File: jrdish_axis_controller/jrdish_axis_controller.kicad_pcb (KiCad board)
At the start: 2 copper layers, 114 parts, among them CN1 KF2EDGR-2.54-9P, CN2 KF2EDGR-2.54-6P, CN3 KF2EDGR-2.54-4P, CN4 KF2EDGR-2.54-4P, CN5 KF2EDGR-2.54-2P, CN6 KF2EDGR-2.54-2P, CN7 SM04B-SRSS-TB (LF)(SN), CN8 SM04B-SRSS-TB (LF)(SN), J1 Conn_ARM_SWD_TagConnect_TC2030, M1 MountingHole_2.7mm_M2.5_ISO14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, Q1 AO3407A, Q2 AO3400A, SW1 DSHP04TSGER, SW2 SS-12F49-G050, U1 STM32G474CET6, U2 ISOW1432BDFMR, U3 MP2322GQH-Z, U4 LTC4311ISC6#TRPBF, U5 LM75BIMX-5/NOPB, U6 M24C64-RMN6TP, X1 NX2016SA-16MHZ-EXS00A-CS07826

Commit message: PCB layout in progress
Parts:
- moved H2 8.57 mm to (163.5, 75.7), turned to 90 degrees
- moved R21 6.60 mm to (128.7, 113.7)
- moved C32 6.60 mm to (132.1, 115.0)
- moved C34 6.60 mm to (137.1, 114.5)
- moved C35 6.60 mm to (135.6, 114.5)
- moved C36 6.60 mm to (130.1, 110.7)
- moved C37 6.60 mm to (133.3, 117.5)
- moved C38 6.60 mm to (134.3, 112.5)
- moved L5 6.60 mm to (129.3, 117.2)
- moved R20 6.60 mm to (128.6, 112.2)
- moved R22 6.60 mm to (131.6, 112.5)
- moved U3 6.60 mm to (133.8, 114.3)
- moved C33 6.45 mm to (138.7, 114.5)
- moved M1 5.68 mm to (129.7, 126.7)
- moved M1 5.55 mm to (181.7, 126.7)
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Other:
- board outline added: 60 x 60 mm

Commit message: Layout no ERC errors
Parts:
- moved R1 22.3 mm to (144.8, 104.8), turned to 180 degrees
- moved H1 20.9 mm to (144.8, 101.5), turned to 90 degrees
- moved Q1 15.3 mm to (128.2, 95.8)
- moved R19 13.0 mm to (135.5, 98.9), turned to 0 degrees
- moved R20 10.8 mm to (138.5, 116.5), turned to 0 degrees
- moved C33 10.4 mm to (128.3, 114.3), turned to 90 degrees
- moved L5 10.1 mm to (138.1, 112.3), turned to 90 degrees
- moved C42 9.95 mm to (166.4, 93.9), turned to -90 degrees
- moved C14 9.78 mm to (141.7, 117.7), turned to -90 degrees
- moved C36 9.36 mm to (138.4, 115.0), turned to 180 degrees
- moved C43 8.43 mm to (178.7, 96.0)
- moved C44 8.33 mm to (136.7, 80.3), turned to -90 degrees
- moved C41 8.18 mm to (167.9, 93.9), turned to -90 degrees
- moved C34 7.13 mm to (129.9, 114.3), turned to 90 degrees
- moved C15 6.22 mm to (145.8, 117.6), turned to -90 degrees
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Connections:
- U1 pad 46: unconnected-(U1-PB9-Pad46) -> RS485_DE_MCU
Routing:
- net GND: track 0.00 -> 122.1 mm, vias 0 -> 56
- net 3.3V: track 0.00 -> 84.9 mm, vias 0 -> 26
- net SCL_MCU: track 0.00 -> 64.9 mm, vias 0 -> 6
- net SDA_MCU: track 0.00 -> 57.6 mm, vias 0 -> 4
- net FAN_MCU: track 0.00 -> 45.5 mm, vias 0 -> 2
- net /RS485/RS485_RX: track 0.00 -> 37.9 mm, vias 0 -> 1
- net /NRST: track 0.00 -> 35.6 mm, vias 0 -> 2
- net /RS485/RS485_TX: track 0.00 -> 34.9 mm
- net /RS485/RS485_CHASSIS: track 0.00 -> 32.6 mm, vias 0 -> 2
- net 12V: track 0.00 -> 31.3 mm, vias 0 -> 9
- net MF_MCU: track 0.00 -> 26.4 mm, vias 0 -> 1
- net PUL_MCU: track 0.00 -> 23.9 mm, vias 0 -> 1
- net Net-(Q1-G): track 0.00 -> 23.5 mm
- net DIR_MCU: track 0.00 -> 22.0 mm, vias 0 -> 1
- net /Power/12V_IN_FUSED: track 0.00 -> 20.0 mm
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- added copper zone on F.Cu, net 12V
- added copper zone on In2.Cu, net 12V
- added copper zone on F.Cu, net 3.3V
- added copper zone on In2.Cu, net 3.3V
- added copper zone on F.Cu, net GND
- added copper zone on In1.Cu, net GND
- added copper zone on F.Cu, net Net-(U3-SW)
- added copper zone on In1.Cu, net RS485_GND
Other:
- copper layers 2 -> 4

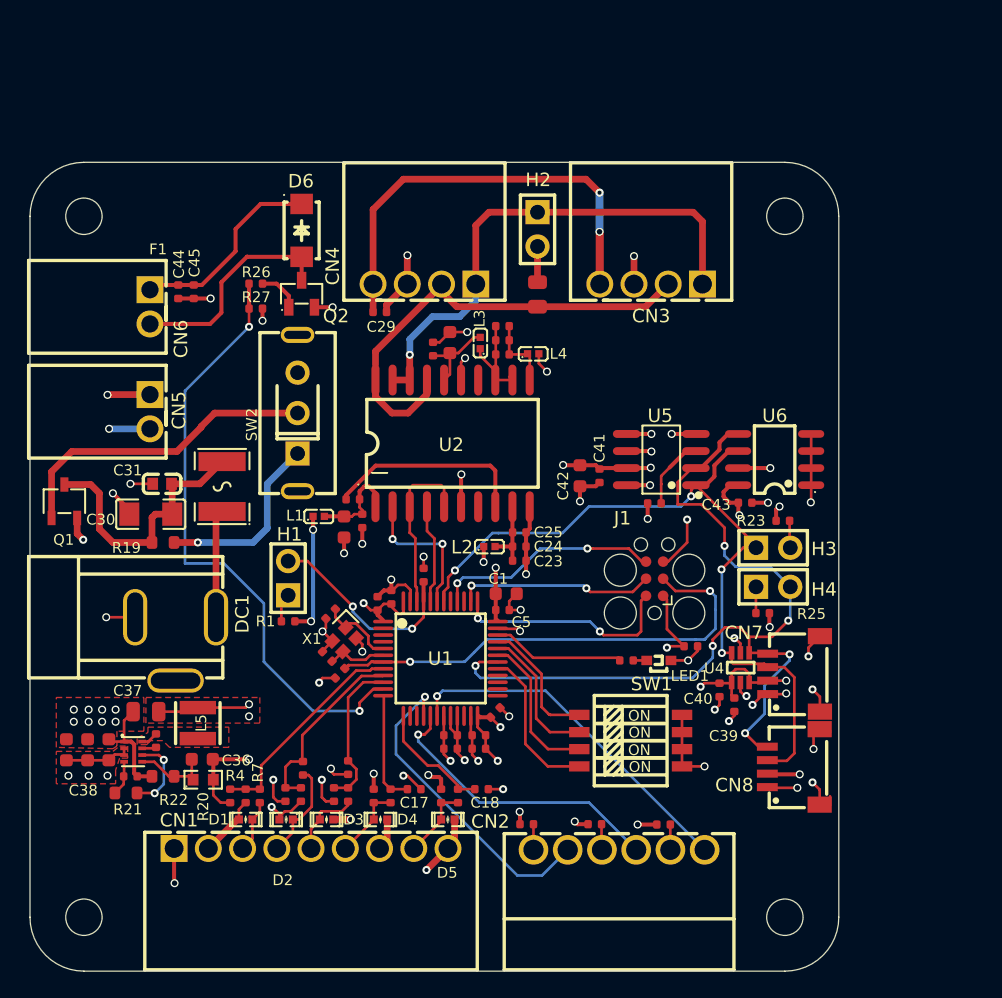
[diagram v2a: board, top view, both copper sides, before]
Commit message: New 64pin version - 2 axes
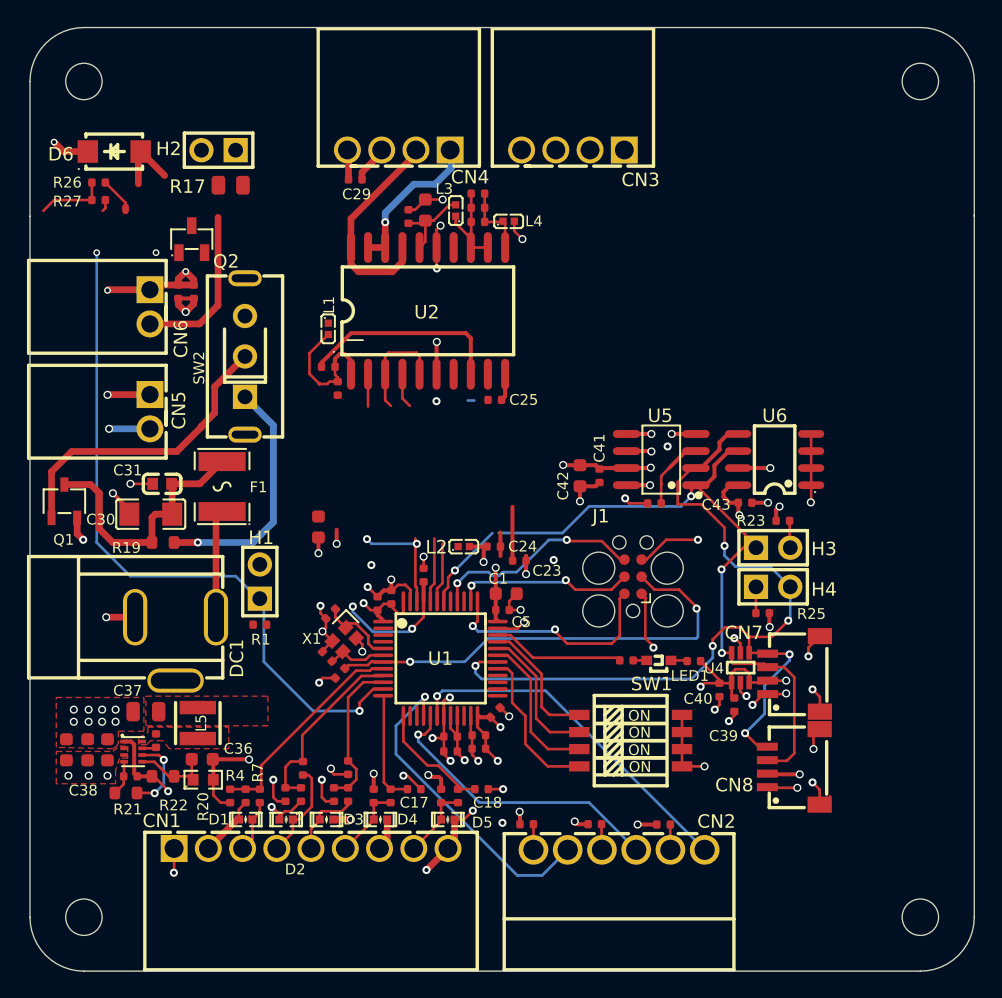
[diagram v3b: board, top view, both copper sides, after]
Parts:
- moved H2 24.4 mm to (139.6, 69.8), turned to 180 degrees
- moved R17 24.2 mm to (140.5, 72.4), turned to 0 degrees
- moved D6 15.1 mm to (131.9, 69.9), turned to 0 degrees
- moved M1 14.2 mm to (191.7, 64.7)
- moved R27 14.2 mm to (130.7, 73.5)
- moved L1 13.9 mm to (147.8, 83.0), turned to -90 degrees
- moved R26 13.9 mm to (130.7, 72.2)
- moved CN3 11.5 mm to (165.9, 69.8)
- moved CN4 10.1 mm to (153.0, 69.8)
- moved M1 10.0 mm to (191.7, 126.7)
- moved M1 10.0 mm to (129.7, 64.7)
- moved C25 10.00 mm to (160.1, 88.3)
- moved C27 10.00 mm to (158.9, 74.1)
- moved L4 10.00 mm to (161.2, 75.1)
- moved C20 10.00 mm to (148.5, 87.5)
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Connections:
- CN3 pad 4: /RS485/RS485_CHASSIS -> unconnected-(CN3-Pad4)
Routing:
- net /RS485/RS485_CHASSIS: track 32.6 -> 2.07 mm, vias 2 -> 0
- net /RS485/RS485_RX: track 37.9 -> 11.1 mm
- net /RS485/RS485_TX: track 34.9 -> 16.3 mm
- net 3.3V: track 84.9 -> 69.7 mm, vias 26 -> 21
- net FAN_MCU: track 45.5 -> 56.5 mm
- net 12V: track 31.3 -> 23.4 mm, vias 9 -> 12
- net Net-(U1-PB8-BOOT0): track 15.3 -> 9.33 mm
- net GND: track 122.1 -> 126.8 mm, vias 56 -> 65
- net Net-(R19-Pad2): track 13.8 -> 18.2 mm
- net USART1_TX_MCU: track 10.7 -> 6.83 mm, vias 2 -> 0
- net RS485_DE_MCU: track 12.7 -> 16.6 mm, vias 0 -> 2
- net Net-(U2-VIO): track 7.49 -> 10.6 mm
- net RS485_GND: track 13.1 -> 10.5 mm, vias 5 -> 4
- net Net-(H2-Pad2): track 2.66 -> 0.00 mm
- net Net-(H1-Pad1): track 2.14 -> 0.00 mm
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- removed copper zone on In2.Cu, net 12V
- removed copper zone on In2.Cu, net 3.3V
- removed copper zone on In1.Cu, net GND
- removed copper zone on In1.Cu, net RS485_GND
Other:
- board size 60 x 60 mm -> 70 x 70 mm
- board text added: "12V"
- board text added: "12V In"
- board text added: "12V Out"
- board text added: "Center Gnd"
- board text added: "Chassis"
- board text added: "Dir+"
- board text added: "Dir-"
- board text added: "Enc 12V"
- board text added: "Enc Gnd"
- board text added: "EncA"
- board text added: "EncB"
- board text added: "EncZ"
- board text added: "Fan"
- board text added: "Gnd"
- board text added: "Lim1 Out"
- board text added: "Lim1 Ret"
- board text added: "Lim2 In"
- board text added: "Lim2 Out"
- board text added: "MF+"
- board text added: "MF-"
- board text added: "N.C."
- board text added: "Pul+"
- board text added: "Pul-"
- board text added: "RS485 In"
- board text added: "RS485 Passthrough"
- board text added: "Rx"
- board text added: "Tx"

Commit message: Continuing layout
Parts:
- removed the C43 at (178.7, 96.0)
- removed the R12 at (162.5, 119.8)
- removed the U6 at (180.9, 92.8)
- added C2: 100nF, PCM_JLCPCB:C_0402, F.Cu at (144.1, 90.3)
- added C22: 10uF, PCM_JLCPCB:C_0603, F.Cu at (163.7, 80.2)
- added C23: 100nF, PCM_JLCPCB:C_0402, F.Cu at (164.0, 79.0)
- added C26: 10uF, PCM_JLCPCB:C_0603, F.Cu at (172.2, 65.6)
- added C27: 100nF, PCM_JLCPCB:C_0402, F.Cu at (170.9, 65.9)
- added C31: 10nF, PCM_JLCPCB:C_0402, F.Cu at (176.5, 81.7)
- added C32: 1uF, PCM_JLCPCB:C_0402, F.Cu at (176.5, 80.6)
- added C33: 10nF, PCM_JLCPCB:C_0402, F.Cu at (176.5, 79.5)
- added C37: 10nF, PCM_JLCPCB:C_0402, F.Cu at (176.8, 66.4)
- added C38: 1uF, PCM_JLCPCB:C_0402, F.Cu at (176.8, 65.3)
- added C39: 10nF, PCM_JLCPCB:C_0402, F.Cu at (176.8, 64.3)
- added C54: 100nF, PCM_JLCPCB:C_0402, F.Cu at (164.4, 108.0)
- added C57: 100nF, PCM_JLCPCB:C_0402, F.Cu at (183.3, 92.0)
- added C58: 100nF, PCM_JLCPCB:C_0402, F.Cu at (182.9, 98.6)
- added C59: 100nF, PCM_JLCPCB:C_0402, F.Cu at (184.6, 101.4)
- added C60: 100nF, PCM_JLCPCB:C_0402, F.Cu at (186.0, 100.9)
- added C61: 100nF, PCM_JLCPCB:C_0402, F.Cu at (188.0, 100.9)
- added C62: 100nF, PCM_JLCPCB:C_0402, F.Cu at (173.7, 119.9)
- added C63: 100nF, PCM_JLCPCB:C_0402, F.Cu at (176.3, 119.9)
- added C64: 100nF, PCM_JLCPCB:C_0402, F.Cu at (178.9, 119.9)
- added C65: 100nF, PCM_JLCPCB:C_0402, F.Cu at (183.5, 117.9)
- added C66: 100nF, PCM_JLCPCB:C_0402, F.Cu at (188.5, 117.9)
- added CN3: KF2EDGR-2.54-9P, MyParts:CONN-TH_9P-P2.54_KF2EDGR-2.54-9P, F.Cu at (179.8, 123.7)
- added CN4: KF2EDGR-2.54-6P, MyParts:CONN-TH_KF2EDGR-2.54-6P, F.Cu at (191.5, 112.6)
- added CN5: KF2EDGR-2.54-3P, MyParts:CONN-TH_3P-P2.54_KF2EDGR-2.54-3P, F.Cu at (191.4, 96.4)
- added CN6: KF2EDGR-2.54-2P, MyParts:CONN-TH_P2.54_KF2EDGR-2.54-2P, F.Cu at (191.4, 85.3)
- added CN9: KF2EDGR-2.54-4P, MyParts:CONN-TH_4P-P2.54_KF2EDGR-2.54-4P, F.Cu at (175.9, 61.6)
- added D10: TPESD0402G05V, MyParts:D0402-BI, F.Cu at (182.9, 121.7)
- added D11: TPESD0402G05V, MyParts:D0402-BI, F.Cu at (187.9, 121.7)
- added D7: TPESD0402G05V, MyParts:D0402-BI, F.Cu at (174.2, 121.7)
- added D8: TPESD0402G05V, MyParts:D0402-BI, F.Cu at (176.8, 121.7)
- added D9: TPESD0402G05V, MyParts:D0402-BI, F.Cu at (179.4, 121.7)
- added L2: BLM15EX331SN1D, MyParts:L0402, F.Cu at (164.1, 77.8)
- added L4: BLM15EX331SN1D, MyParts:L0402, F.Cu at (174.9, 80.4)
- added L6: BLM15EX331SN1D, MyParts:L0402, F.Cu at (174.3, 66.4)
- added L8: BLM15EX331SN1D, MyParts:L0402, F.Cu at (179.0, 66.5)
- added Q3: 2N7002, Package_TO_SOT_SMD:SOT-23, F.Cu at (187.0, 84.7)
- added R14: 330Ω, PCM_JLCPCB:R_0402, F.Cu at (151.6, 121.3)
- added R19: 4.7kΩ, PCM_JLCPCB:R_0402, F.Cu at (164.0, 76.2)
- added R29: 1kΩ, PCM_JLCPCB:R_0402, F.Cu at (185.5, 83.2)
- added R30: 10kΩ, PCM_JLCPCB:R_0402, F.Cu at (189.3, 86.1)
- added R31: 4.7kΩ, PCM_JLCPCB:R_0402, F.Cu at (174.7, 117.9)
- added R32: 4.7kΩ, PCM_JLCPCB:R_0402, F.Cu at (177.3, 117.9)
- added R33: 4.7kΩ, PCM_JLCPCB:R_0402, F.Cu at (179.9, 117.9)
- added R34: 100Ω, PCM_JLCPCB:R_0402, F.Cu at (174.7, 119.9)
- added R35: 100Ω, PCM_JLCPCB:R_0402, F.Cu at (177.3, 119.9)
- added R36: 100Ω, PCM_JLCPCB:R_0402, F.Cu at (179.9, 119.9)
- added R37: 10kΩ, PCM_JLCPCB:R_0402, F.Cu at (182.4, 119.9)
- added R38: 10kΩ, PCM_JLCPCB:R_0402, F.Cu at (187.4, 119.9)
- added R39: 100Ω, PCM_JLCPCB:R_0402, F.Cu at (183.5, 119.9)
- added R40: 100Ω, PCM_JLCPCB:R_0402, F.Cu at (188.5, 119.9)
- added R41: 330Ω, PCM_JLCPCB:R_0402, F.Cu at (189.5, 117.3)
- added R42: 330Ω, PCM_JLCPCB:R_0402, F.Cu at (188.8, 113.8)
- added R43: 330Ω, PCM_JLCPCB:R_0402, F.Cu at (188.8, 108.8)
- added U3: ISOW1432BDFMR, MyParts:SOIC-20_L12.8-W7.5-P1.27-LS10.3-BL, F.Cu at (171.6, 73.0)
- added U7: W25Q32JVSSIQ_C179173, MyParts:SOIC-8_L5.3-W5.3-P1.27-LS8.0-BL, F.Cu at (167.9, 104.9)
- added U8: SP3232EEY-L/TR, MyParts:TSSOP-16_L5.0-W4.4-P0.65-LS6.4-BL, F.Cu at (186.1, 96.5)
- R15, R16: value 1.5kΩ -> 330Ω
- U1: value STM32G474CET6 -> STM32G474RET6; footprint MyParts:LQFP-48_L7.0-W7.0-P0.50-LS9.0-BL -> MyParts:LQFP-64_L10.0-W10.0-P0.50-LS12.0-BL
- moved R26 46.6 mm to (188.7, 58.3), turned to -90 degrees
- moved C50 44.5 mm to (191.3, 68.5)
- moved C51 44.1 mm to (192.3, 68.5)
- moved CN8 44.1 mm to (197.8, 67.4)
- moved U5 44.0 mm to (193.8, 67.0)
- moved CN7 43.2 mm to (197.9, 75.3)
- moved H4 42.3 mm to (189.9, 60.9)
- moved H3 36.3 mm to (189.8, 64.1), turned to 180 degrees
- moved R25 34.0 mm to (195.4, 71.4), turned to 90 degrees
- moved R24 32.0 mm to (189.1, 66.2), turned to 180 degrees
- moved C53 28.0 mm to (188.8, 77.2), turned to 0 degrees
- moved U6 26.6 mm to (191.1, 73.8)
- moved C52 25.9 mm to (186.8, 76.2)
- moved C12 24.4 mm to (167.5, 84.4)
- moved CN11 20.7 mm to (147.0, 61.6)
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- renumbered C9 to C10, C10 to C11, C13 to C12, C11 to C13, C12 to C14, C14 to C15, C15 to C16, C16 to C17, C17 to C18, C18 to C19, C19 to C20, C20 to C21, C21 to C24, C22 to C25, C23 to C28, C24 to C29, C2 to C3, C25 to C30, C26 to C34, C27 to C35, C28 to C36, C3 to C4, C29 to C40, C30 to C41, C31 to C42, C32 to C43, C33 to C44, C34 to C45, C35 to C46, C36 to C47, C37 to C48, C38 to C49, C4 to C5, C39 to C50, C40 to C51, C41 to C52, C42 to C53, C44 to C55, C45 to C56, C5 to C6, C6 to C7, C7 to C8, C8 to C9, CN4 to CN10, CN3 to CN11, CN6 to CN12, CN5 to CN13, CN8 to CN7, CN7 to CN8, L2 to L3, L3 to L5, L4 to L7, L5 to L9, R13 to R12, R14 to R13, R19 to R20, R20 to R21, R21 to R22, R22 to R23, R23 to R24, R24 to R25, R25 to R26, R26 to R27, R27 to R28, U3 to U4, U4 to U5, U5 to U6
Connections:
- net /Axis Control/LIM1_OUT renamed /Axis Control - 1/LIM1_SW1_OUT
- net /Axis Control/LIM2_OUT renamed /Axis Control - 1/LIM1_SW2_OUT
- net ENC_A renamed ENC1_A
- net ENC_B renamed ENC1_B
- net ENC_Z renamed ENC1_Z
- C1 pad 1: 3.3V -> 3V3
- C10 pad 1: 3.3V -> 3V3
- C12 pad 1: 3.3V -> 3V3
- C15 pad 1: ENC_A_MCU -> ENC1_A_MCU
- C16 pad 1: ENC_B_MCU -> ENC1_B_MCU
- C17 pad 1: ENC_Z_MCU -> ENC1_Z_MCU
- C18 pad 1: LIMIT_SW1_MCU -> LIMIT1_SW1_MCU
- C19 pad 1: LIMIT_SW2_MCU -> LIMIT1_SW2_MCU
- C3 pad 1: 3.3V -> 3V3
- C4 pad 1: 3.3V -> 3V3
- C47 pad 1: 3.3V -> 3V3
- C48 pad 1: 3.3V -> 3V3
- C5 pad 1: 3.3V -> 3V3
- C50 pad 1: 3.3V -> 3V3
- C51 pad 1: 3.3V -> 3V3
- C52 pad 1: 3.3V -> 3V3
- C53 pad 1: 3.3V -> 3V3
- C6 pad 1: 3.3V -> 3V3
- C7 pad 1: 3.3V -> 3V3
- C8 pad 1: 3.3V -> 3V3
- C9 pad 1: 3.3V -> 3V3
- CN10 pad 1: /RS485/RS485_RX -> /RS485/RS485_1_TX
- CN10 pad 2: /RS485/RS485_TX -> /RS485/RS485_1_RX
- CN11 pad 1: /RS485/RS485_RX -> /RS485/RS485_1_TX
- CN11 pad 2: /RS485/RS485_TX -> /RS485/RS485_1_RX
- CN2 pad 2: PUL_MCU -> PUL1_MCU
- CN2 pad 4: DIR_MCU -> DIR1_MCU
- CN2 pad 6: MF_MCU -> ENABLE1_MCU
- CN7 pad 2: 3.3V -> 3V3
- CN8 pad 2: 3.3V -> 3V3
- H2 pad 1: /RS485/RS485_RX -> /RS485/RS485_1_RX
- J1 pad 1: 3.3V -> 3V3
- L1 pad 1: 3.3V -> 3V3
- L3 pad 1: 3.3V -> 3V3
- L7 pad 2: RS485_GND -> GND
- L9 pad 2: 3.3V -> 3V3
- R1 pad 1: 3.3V -> 3V3
- R10 pad 1: 3.3V -> 3V3
- R11 pad 1: 3.3V -> 3V3
- R12 pad 2: LIMIT_SW1_MCU -> LIMIT1_SW1_MCU
- R13 pad 2: LIMIT_SW2_MCU -> LIMIT1_SW2_MCU
- R15 pad 1: 12V -> 3V3
- R16 pad 1: 12V -> 3V3
- R17 pad 2: /RS485/RS485_TX -> /RS485/RS485_1_TX
- R21 pad 2: 3.3V -> 3V3
- R24 pad 1: 3.3V -> 3V3
- R25 pad 2: 3.3V -> 3V3
- R26 pad 1: 3.3V -> 3V3
- R4 pad 1: ENC_A_MCU -> ENC1_A_MCU
- R4 pad 2: 3.3V -> 3V3
- R5 pad 1: ENC_B_MCU -> ENC1_B_MCU
- R5 pad 2: 3.3V -> 3V3
- R6 pad 1: ENC_Z_MCU -> ENC1_Z_MCU
- R6 pad 2: 3.3V -> 3V3
- R7 pad 2: ENC_A_MCU -> ENC1_A_MCU
- R8 pad 2: ENC_B_MCU -> ENC1_B_MCU
- R9 pad 2: ENC_Z_MCU -> ENC1_Z_MCU
- SW1 pad 1: Net-(SW1-A1) -> /ADDR0
- SW1 pad 2: Net-(SW1-A2) -> /ADDR1
- SW1 pad 3: Net-(SW1-A3) -> /ADDR2
- SW1 pad 4: Net-(SW1-A4) -> /CONFIG_SW
- U1 pad 1: 3.3V -> 3V3
- U1 pad 10: ENC_Z_MCU -> unconnected-(U1-PC2-Pad10)
- U1 pad 11: FAN_MCU -> ENC2_Z_MCU
- U1 pad 12: LIMIT_SW1_MCU -> ENC1_A_MCU
- U1 pad 13: LIMIT_SW2_MCU -> ENC1_B_MCU
- U1 pad 14: unconnected-(U1-PA6-Pad14) -> ENC1_Z_MCU
- U1 pad 15: unconnected-(U1-PA7-Pad15) -> GND
- U1 pad 16: PUL_MCU -> 3V3
- U1 pad 17: DIR_MCU -> LIMIT1_SW1_MCU
- U1 pad 18: MF_MCU -> LIMIT1_SW2_MCU
- U1 pad 19: GND -> LIMIT2_SW1_MCU
- U1 pad 2: unconnected-(U1-PC13-Pad2) -> FAN_MCU
- U1 pad 20: 3.3V -> PUL1_MCU
- U1 pad 21: 3.3V -> LIMIT2_SW2_MCU
- U1 pad 22: unconnected-(U1-PB10-Pad22) -> DIR1_MCU
- U1 pad 23: GND -> ENABLE1_MCU
- U1 pad 24: 3.3V -> PUL2_MCU
- U1 pad 25: unconnected-(U1-PB11-Pad25) -> DIR2_MCU
- U1 pad 26: unconnected-(U1-PB12-Pad26) -> ENABLE2_MCU
- U1 pad 27: unconnected-(U1-PB13-Pad27) -> GND
- U1 pad 28: unconnected-(U1-PB14-Pad28) -> 3V3
- U1 pad 29: Net-(SW1-A4) -> 3V3
- U1 pad 30: SCL_MCU -> RS232_RX_MCU
- U1 pad 31: Net-(SW1-A3) -> GND
- U1 pad 32: Net-(SW1-A2) -> 3V3
- U1 pad 33: Net-(SW1-A1) -> RS232_TX_MCU
- U1 pad 34: Net-(U1-PA12) -> FLASH_CS_MCU
- U1 pad 35: GND -> SPI2_SCK_MCU
- U1 pad 36: 3.3V -> SPI2_MISO_MCU
- U1 pad 37: /SWDIO -> SPI2_MOSI_MCU
- U1 pad 38: /SWCLK -> SCL_MCU
- U1 pad 39: unconnected-(U1-PA15-Pad39) -> SDA_MCU
- U1 pad 40: /SWO -> unconnected-(U1-PC8-Pad40)
- U1 pad 42: SDA_MCU -> /CONFIG_SW
- U1 pad 43: USART1_TX_MCU -> /ADDR2
- U1 pad 44: USART1_RX_MCU -> /ADDR1
- U1 pad 45: Net-(U1-PB8-BOOT0) -> /ADDR0
- U1 pad 46: RS485_DE_MCU -> Net-(U1-PA12)
- U1 pad 48: 3.3V -> 3V3
- U1 pad 8: ENC_A_MCU -> ENC2_A_MCU
- U1 pad 9: ENC_B_MCU -> ENC2_B_MCU
- U2 pad 17: /RS485/RS485_TX -> /RS485/RS485_1_TX
- U2 pad 18: /RS485/RS485_RX -> /RS485/RS485_1_RX
- U2 pad 19: /RS485/RS485_RX -> /RS485/RS485_1_RX
- U2 pad 2: USART1_TX_MCU -> RS485_1_TX_MCU
- U2 pad 20: /RS485/RS485_TX -> /RS485/RS485_1_TX
- U2 pad 3: RS485_DE_MCU -> RS485_1_DE_MCU
- U2 pad 4: USART1_RX_MCU -> RS485_1_RX_MCU
- U2 pad 5: RS485_DE_MCU -> RS485_1_DE_MCU
- U5 pad 1: 3.3V -> 3V3
- U5 pad 3: 3.3V -> 3V3
- U6 pad 7: 3.3V -> 3V3
- U6 pad 8: 3.3V -> 3V3
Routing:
- net GND: track 126.8 -> 0.00 mm, vias 65 -> 0
- net 3.3V: track 69.7 -> 0.00 mm, vias 21 -> 0
- net SCL_MCU: track 64.9 -> 0.00 mm, vias 6 -> 0
- net SDA_MCU: track 57.6 -> 0.00 mm, vias 4 -> 0
- net FAN_MCU: track 56.5 -> 0.00 mm, vias 2 -> 0
- net /NRST: track 34.4 -> 0.00 mm, vias 2 -> 0
- net MF_MCU: track 26.4 -> 0.00 mm, vias 1 -> 0
- net PUL_MCU: track 23.9 -> 0.00 mm, vias 1 -> 0
- net 12V: track 23.4 -> 0.00 mm, vias 12 -> 0
- net Net-(Q1-G): track 22.5 -> 0.00 mm
- net DIR_MCU: track 22.0 -> 0.00 mm, vias 1 -> 0
- net /Power/12V_IN_FUSED: track 20.0 -> 0.00 mm
- net Net-(R20-Pad2): track 18.2 -> 0.00 mm, vias 1 -> 0
- net Net-(D6-A): track 17.1 -> 0.00 mm
- net /SWDIO: track 17.1 -> 0.00 mm, vias 2 -> 0
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- added copper zone on F.Cu, net 3V3
- removed copper zone on F.Cu, net 3.3V
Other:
- board size 70 x 70 mm -> 85 x 80 mm
- board text added: "flash"

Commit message: Continuing layout
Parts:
- moved U7 6.23 mm to (173.8, 102.8)
- moved C54 6.23 mm to (170.2, 105.8)
- moved SW1 6.09 mm to (173.7, 94.8)
- moved H2 5.01 mm to (144.4, 65.0), turned to 180 degrees
- moved M1 5.00 mm to (196.4, 128.6)
- moved M1 5.00 mm to (196.4, 56.6)
- moved R17 3.03 mm to (143.4, 68.6), turned to -90 degrees
- moved R27 1.66 mm to (126.4, 61.4), turned to 180 degrees
- moved R21 1.64 mm to (127.5, 107.8)
- moved C44 1.60 mm to (117.3, 105.6)
- moved C45 1.60 mm to (118.9, 105.6)
- moved C46 1.60 mm to (120.4, 105.6)
- moved C48 1.60 mm to (123.3, 102.8)
- moved L9 1.60 mm to (127.1, 103.6)
- moved C43 1.60 mm to (124.0, 104.9)
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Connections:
- L7 pad 2: GND -> RS485_GND
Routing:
- net GND: track 0.00 -> 111.4 mm, vias 0 -> 193
- net SDA_MCU: track 0.00 -> 91.9 mm
- net SCL_MCU: track 0.00 -> 89.9 mm, vias 0 -> 3
- net 3V3: track 0.00 -> 78.1 mm, vias 0 -> 46
- net RS232_RX_MCU: track 0.00 -> 68.7 mm, vias 0 -> 2
- net 12V: track 0.00 -> 64.0 mm, vias 0 -> 7
- net LIMIT2_SW1_MCU: track 0.00 -> 63.9 mm
- net LIMIT2_SW2_MCU: track 0.00 -> 55.7 mm, vias 0 -> 2
- net PUL2_MCU: track 0.00 -> 51.7 mm
- net RS232_TX_MCU: track 0.00 -> 50.9 mm
- net ENC2_Z_MCU: track 0.00 -> 50.2 mm, vias 0 -> 2
- net ENABLE2_MCU: track 0.00 -> 48.5 mm, vias 0 -> 2
- net DIR2_MCU: track 0.00 -> 48.1 mm
- net ENC2_A_MCU: track 0.00 -> 46.1 mm, vias 0 -> 2
- net ENC2_B_MCU: track 0.00 -> 45.8 mm, vias 0 -> 2
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- added copper zone on In2.Cu, net 12V
- added copper zone on In2.Cu, net 3V3
- added copper zone on B.Cu, net GND
- added copper zone on In1.Cu, net GND
- added copper zone on B.Cu, net RS485_GND
- added copper zone on F.Cu, net RS485_GND
- added copper zone on In1.Cu, net RS485_GND
- added copper zone on In2.Cu, net RS485_GND
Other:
- board text added: "12V IN Center Gnd"
- board text added: "12V OUT 12V-Gnd"
- board text added: "1PPS + -"
- board text added: "ADDR0"
- board text added: "ADDR1"
- board text added: "ADDR2"
- board text added: "CONFIG"
- board text added: "FAN 12V-Gnd"
- board text added: "I2C"
- board text added: "I2C Pull-ups"
- board text added: "ON"
- board text added: "RS232"
- board text added: "TX-RX-GND"
- board text removed: "Center Gnd"
